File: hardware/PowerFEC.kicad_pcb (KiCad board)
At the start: 2 copper layers, 24 x 27.9 mm, 27 parts, among them J1 105444-0001, J2 B2B-XH-A, U1 PIC16F1455, U2 AP22652, U3 ZXCT1009, U4 MCP3423

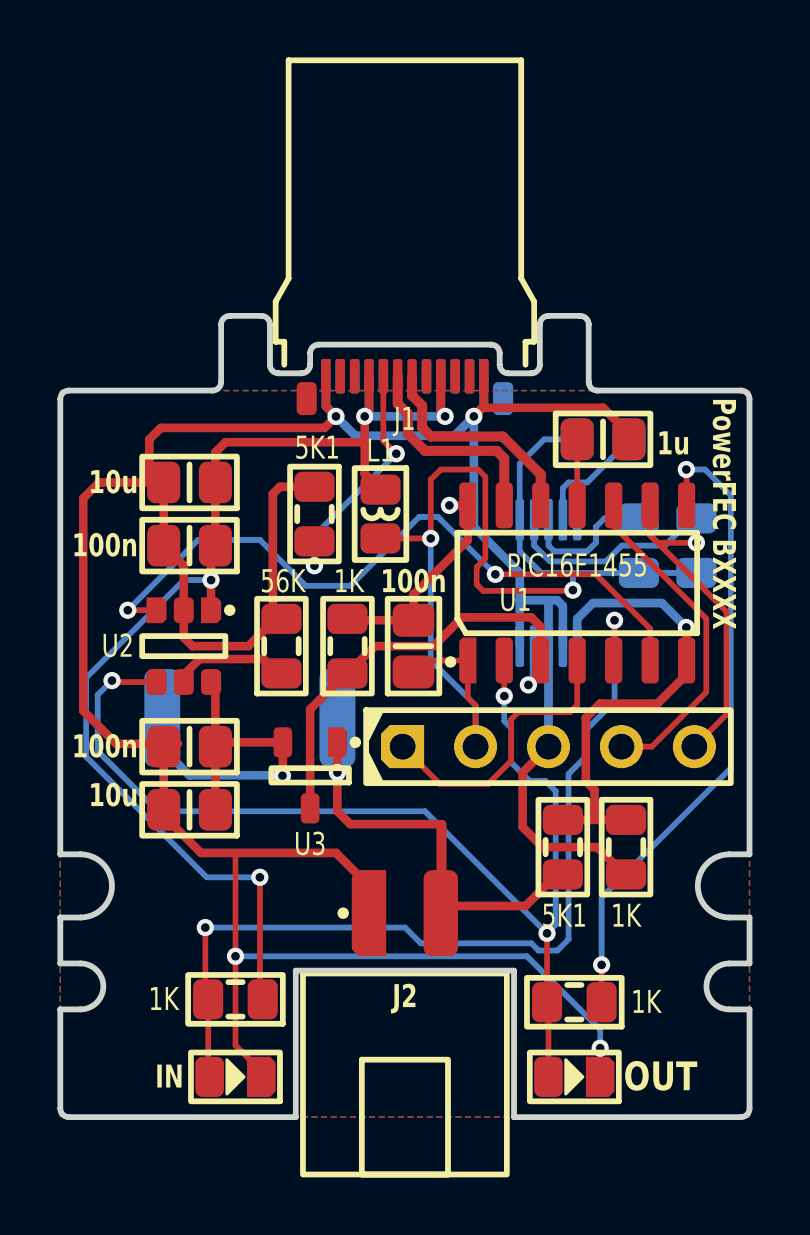
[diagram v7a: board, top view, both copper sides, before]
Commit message: Changed ADC to MCP3422
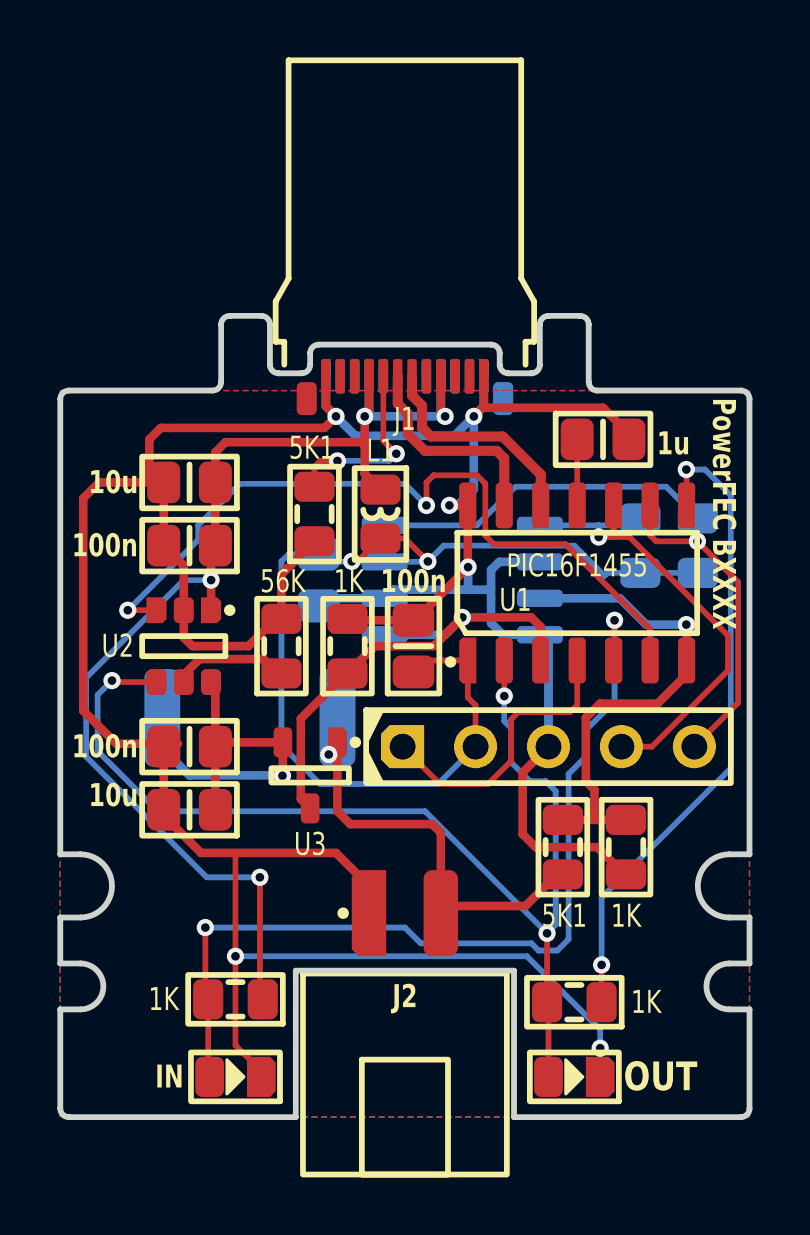
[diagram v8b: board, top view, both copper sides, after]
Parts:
- removed U4: MCP3423, Medo64:U ADC 18bit 2ch [MCP3423] (MSOP-10)
- added U?: MCP3422, Medo64:U ADC 18bit 2ch [MCP3422] (SOIC-8), B.Cu at (34.0, 29.2)
- moved C4 11.0 mm to (29.0, 29.2), turned to -90 degrees
- moved R7 0.05 mm to (40.2, 28.0)
- moved R8 0.05 mm to (42.2, 28.0)
- turned R6 to 90 degrees
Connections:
- net ICSP_CLK renamed ICSP_CLK/SDA
- net ICSP_DAT renamed ICSP_DAT/SCL
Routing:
- net GND: track 130.4 -> 124.7 mm, vias 5 -> 6
- net Vout: track 17.6 -> 14.1 mm
- net ICSP_CLK/SDA: track 19.8 -> 23.1 mm
- net POWER_EN: track 24.6 -> 26.9 mm
- net A_CC: track 8.82 -> 6.62 mm
- net Iadc: track 16.2 -> 17.4 mm
- net 5V: track 38.3 -> 37.4 mm
- net ICSP_DAT/SCL: track 16.5 -> 16.7 mm, vias 0 -> 1
